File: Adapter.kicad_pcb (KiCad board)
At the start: 6 copper layers, 164.7 x 117 mm, 203 parts, among them J1 GD820HTX75P6HB, J2 2-338069-0, U1 R-78E3.3-1.0, U11 LMV7219M5, U2 LM1117GS-3.3, U5 ADuM1200AR

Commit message: Добавил температурные контуры звщиты
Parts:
- added C50: 0.1u, Capacitor_SMD:C_0805_2012Metric_Pad1.18x1.45mm_HandSolder, B.Cu at (121.2, 108.1)
- added C51: 0.1u, Capacitor_SMD:C_0805_2012Metric_Pad1.18x1.45mm_HandSolder, B.Cu at (121.2, 115.5)
- added C52: 0.1u, Capacitor_SMD:C_0805_2012Metric_Pad1.18x1.45mm_HandSolder, B.Cu at (117.1, 115.5)
- added C53: 0.1u, Capacitor_SMD:C_0805_2012Metric_Pad1.18x1.45mm_HandSolder, B.Cu at (168.1, 108.2)
- added C54: 0.1u, Capacitor_SMD:C_0805_2012Metric_Pad1.18x1.45mm_HandSolder, B.Cu at (168.1, 115.6)
- added C55: 0.1u, Capacitor_SMD:C_0805_2012Metric_Pad1.18x1.45mm_HandSolder, B.Cu at (164.1, 115.6)
- added C56: 0.1u, Capacitor_SMD:C_0805_2012Metric_Pad1.18x1.45mm_HandSolder, B.Cu at (215.4, 108.0)
- added C75: 0.1u, Capacitor_SMD:C_0805_2012Metric_Pad1.18x1.45mm_HandSolder, B.Cu at (215.4, 115.3)
- added C76: 0.1u, Capacitor_SMD:C_0805_2012Metric_Pad1.18x1.45mm_HandSolder, B.Cu at (211.3, 115.3)
- added R56: 1k, Resistor_SMD:R_0805_2012Metric_Pad1.20x1.40mm_HandSolder, B.Cu at (121.2, 117.8)
- added R57: 1k, Resistor_SMD:R_0805_2012Metric_Pad1.20x1.40mm_HandSolder, B.Cu at (117.1, 108.1)
- added R58: 1k, Resistor_SMD:R_0805_2012Metric_Pad1.20x1.40mm_HandSolder, B.Cu at (117.1, 120.1)
- added R59: 1k, Resistor_SMD:R_0805_2012Metric_Pad1.20x1.40mm_HandSolder, B.Cu at (117.1, 117.8)
- added R60: 1k, Resistor_SMD:R_0805_2012Metric_Pad1.20x1.40mm_HandSolder, B.Cu at (168.1, 117.9)
- added R63: 1k, Resistor_SMD:R_0805_2012Metric_Pad1.20x1.40mm_HandSolder, B.Cu at (164.1, 108.2)
- added R64: 1k, Resistor_SMD:R_0805_2012Metric_Pad1.20x1.40mm_HandSolder, B.Cu at (164.1, 120.1)
- added R65: 1k, Resistor_SMD:R_0805_2012Metric_Pad1.20x1.40mm_HandSolder, B.Cu at (164.1, 117.9)
- added R70: 1k, Resistor_SMD:R_0805_2012Metric_Pad1.20x1.40mm_HandSolder, B.Cu at (215.4, 117.6)
- added R72: 1k, Resistor_SMD:R_0805_2012Metric_Pad1.20x1.40mm_HandSolder, B.Cu at (211.3, 108.0)
- added R75: 1k, Resistor_SMD:R_0805_2012Metric_Pad1.20x1.40mm_HandSolder, B.Cu at (211.3, 119.9)
- added R76: 1k, Resistor_SMD:R_0805_2012Metric_Pad1.20x1.40mm_HandSolder, B.Cu at (211.3, 117.6)
- added U3: LMV331, Package_TO_SOT_SMD:SOT-23-5_HandSoldering, B.Cu at (119.1, 111.8)
- added U4: LMV331, Package_TO_SOT_SMD:SOT-23-5_HandSoldering, B.Cu at (166.1, 111.8)
- added U6: LMV331, Package_TO_SOT_SMD:SOT-23-5_HandSoldering, B.Cu at (213.4, 111.5)
- C2, C21, C23, C25, C32, C33: moved to B.Cu
- moved C33 288.8 mm to (233.9, 139.2), turned to 90 degrees
- moved C32 280.1 mm to (231.9, 132.6), turned to 0 degrees
- moved U1 278.7 mm to (230.7, 135.5), turned to -90 degrees
- moved R39 255.3 mm to (190.0, 59.2)
- moved R40 255.3 mm to (190.0, 61.7)
- moved C2 231.9 mm to (195.6, 54.3), turned to -90 degrees
- moved C25 217.3 mm to (204.2, 140.2), turned to -90 degrees
- moved C26 215.3 mm to (204.5, 134.4), turned to -90 degrees
- moved R4 211.1 mm to (202.2, 134.4), turned to 90 degrees
- moved C45 210.6 mm to (190.0, 53.8)
- moved C46 210.6 mm to (190.0, 56.4)
- moved C23 174.8 mm to (157.2, 140.2), turned to -90 degrees
- moved C24 171.9 mm to (157.5, 134.4), turned to -90 degrees
- moved R3 166.1 mm to (155.2, 134.4), turned to 90 degrees
- moved C21 135.6 mm to (110.2, 140.2), turned to -90 degrees
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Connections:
- C1 pad 2: GND -> T1
- C12 pad 2: GND -> T1
- C13 pad 2: GND -> T1
- C16 pad 2: GND -> T1
- C18 pad 2: GND -> T1
- C19 pad 2: GND -> T1
- C2 pad 2: GND -> T1
- C21 pad 2: GND -> T1
- C22 pad 2: GND -> T1
- C23 pad 2: GND -> T1
- C24 pad 1: Current_A_out -> Current_B_out
- C24 pad 2: GND -> T1
- C25 pad 2: GND -> T1
- C26 pad 1: Current_A_out -> Current_C_out
- C26 pad 2: GND -> T1
- C29 pad 1: T3 -> T5
- C32 pad 2: GND -> T1
- C33 pad 2: GND -> T1
- C34 pad 2: GND -> T1
- C35 pad 2: GND -> T1
- C37 pad 2: GND -> T1
- C38 pad 2: GND -> T1
- C39 pad 2: GND -> T1
- C4 pad 2: GND -> T1
- C41 pad 2: GND -> T1
- C42 pad 2: GND -> T1
- C45 pad 2: GND -> T1
- C46 pad 2: GND -> T1
- C47 pad 2: GND -> T1
- C48 pad 2: GND -> T1
- C5 pad 2: GND -> T1
- C57 pad 1: GND -> T1
- C58 pad 1: GND -> T1
- C59 pad 1: GND -> T1
- C6 pad 2: GND -> T1
- C60 pad 1: GND -> T1
- C63 pad 1: GND -> T1
- C64 pad 1: GND -> T1
- C65 pad 1: GND -> T1
- C66 pad 1: GND -> T1
- C69 pad 1: GND -> T1
- C7 pad 2: GND -> T1
- C70 pad 1: GND -> T1
- C71 pad 1: GND -> T1
- C72 pad 1: GND -> T1
- C8 pad 2: GND -> T1
- C9 pad 2: GND -> T1
- D10 pad 1: GND -> T1
- D11 pad 3: GND -> T1
- D13 pad 1: GND -> T1
- D14 pad 3: GND -> T1
- D15 pad 3: GND -> T1
- D16 pad 1: GND -> T1
- D17 pad 1: GND -> T1
- D18 pad 1: GND -> T1
- D19 pad 1: GND -> T1
- D2 pad 2: GND -> T1
- D2 pad 3: GND -> T1
- D2 pad 5: GND -> T1
- D20 pad 5: GND -> T1
- D3 pad 2: GND -> T1
- D3 pad 3: GND -> T1
- D3 pad 5: GND -> T1
- D31 pad 16: GND -> T1
- D31 pad 9: GND -> T1
- D32 pad 16: GND -> T1
- D32 pad 9: GND -> T1
- D37 pad 16: GND -> T1
- D37 pad 9: GND -> T1
- D38 pad 16: GND -> T1
- D38 pad 9: GND -> T1
- D4 pad 1: GND -> T1
- D43 pad 1: GND -> T1
- D44 pad 16: GND -> T1
- D44 pad 9: GND -> T1
- D5 pad 4: unconnected-(D5-DI-Pad4) -> Net-(D1-Y)
- D5 pad 5: GND -> T1
- D6 pad 2: GND -> T1
- D6 pad 3: GND -> T1
- D6 pad 5: GND -> T1
- D64 pad 16: GND -> T1
- D64 pad 9: GND -> T1
- D7 pad 2: GND -> T1
- D7 pad 3: GND -> T1
- D7 pad 5: GND -> T1
- D8 pad 2: GND -> T1
- D8 pad 3: GND -> T1
- D8 pad 5: GND -> T1
- D9 pad 2: GND -> T1
- D9 pad 3: GND -> T1
- D9 pad 5: GND -> T1
- J2 pad 18: GND -> T1
- R28 pad 2: T4 -> T6
- R3 pad 2: Current_A_out -> Current_B_out
- R4 pad 2: Current_A_out -> Current_C_out
- U1 pad 2: GND -> T1
- U11 pad 4: T3 -> T5
- U5 pad 5: GND -> T1
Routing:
- net GND: track 118.4 -> 0.00 mm, vias 2 -> 0
- net (no net): track 582.5 -> 697.8 mm
- net T1: track 0.00 -> 3.07 mm, vias 0 -> 2

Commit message: Убрал питание 3.3В
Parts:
- removed C50, C51, C52, C53, C54, C55, C56, C75, C76: 0.1u, Capacitor_SMD:C_0805_2012Metric_Pad1.18x1.45mm_HandSolder
- removed R56, R57, R58, R59, R60, R63, R64, R65, R70, R72, R75, R76: 1k, Resistor_SMD:R_0805_2012Metric_Pad1.20x1.40mm_HandSolder
- removed U3, U4, U6: LMV331, Package_TO_SOT_SMD:SOT-23-5_HandSoldering
- added D1: SN74AHC1G08DBVR, Package_TO_SOT_SMD:SOT-23-5_HandSoldering, F.Cu at (184.1, 56.7)
- U11: value LMV7219M5 -> LMV7239M5/NOPB
- U2: value LM1117GS-3.3 -> LM1117GS-5.0
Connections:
- net +3.3VA renamed +5VP
- C1 pad 1: +3V3 -> +5V
- C1 pad 2: T1 -> GND
- C12 pad 2: T1 -> GND
- C13 pad 2: T1 -> GND
- C16 pad 2: T1 -> GND
- C18 pad 2: T1 -> GND
- C19 pad 2: T1 -> GND
- C2 pad 1: +3V3 -> +5V
- C2 pad 2: T1 -> GND
- C21 pad 2: T1 -> GND
- C22 pad 2: T1 -> GND
- C23 pad 2: T1 -> GND
- C24 pad 2: T1 -> GND
- C25 pad 2: T1 -> GND
- C26 pad 2: T1 -> GND
- C32 pad 2: T1 -> GND
- C33 pad 1: +3V3 -> +5V
- C33 pad 2: T1 -> GND
- C34 pad 1: +3V3 -> +5V
- C34 pad 2: T1 -> GND
- C35 pad 1: +3V3 -> +5V
- C35 pad 2: T1 -> GND
- C37 pad 2: T1 -> GND
- C38 pad 2: T1 -> GND
- C39 pad 2: T1 -> GND
- C4 pad 2: T1 -> GND
- C41 pad 1: +3V3 -> +5V
- C41 pad 2: T1 -> GND
- C42 pad 1: +3V3 -> +5V
- C42 pad 2: T1 -> GND
- C45 pad 2: T1 -> GND
- C46 pad 2: T1 -> GND
- C47 pad 2: T1 -> GND
- C48 pad 2: T1 -> GND
- C5 pad 1: +3V3 -> +5V
- C5 pad 2: T1 -> GND
- C57 pad 1: T1 -> GND
- C57 pad 2: +3V3 -> +5V
- C58 pad 1: T1 -> GND
- C58 pad 2: +3V3 -> +5V
- C59 pad 1: T1 -> GND
- C6 pad 1: +3V3 -> +5V
- C6 pad 2: T1 -> GND
- C60 pad 1: T1 -> GND
- C63 pad 1: T1 -> GND
- C63 pad 2: +3V3 -> +5V
- C64 pad 1: T1 -> GND
- C64 pad 2: +3V3 -> +5V
- C65 pad 1: T1 -> GND
- C66 pad 1: T1 -> GND
- C69 pad 1: T1 -> GND
- C69 pad 2: +3V3 -> +5V
- C7 pad 1: +3V3 -> +5V
- C7 pad 2: T1 -> GND
- C70 pad 1: T1 -> GND
- C70 pad 2: +3V3 -> +5V
- C71 pad 1: T1 -> GND
- C72 pad 1: T1 -> GND
- C8 pad 1: +3V3 -> +5V
- C8 pad 2: T1 -> GND
- C9 pad 2: T1 -> GND
- D10 pad 1: T1 -> GND
- D11 pad 3: T1 -> GND
- D13 pad 1: T1 -> GND
- D14 pad 3: T1 -> GND
- D15 pad 3: T1 -> GND
- D16 pad 1: T1 -> GND
- D17 pad 1: T1 -> GND
- D18 pad 1: T1 -> GND
- D19 pad 1: T1 -> GND
- D2 pad 2: T1 -> GND
- D2 pad 3: T1 -> GND
- D2 pad 5: T1 -> GND
- D2 pad 8: +3V3 -> +5V
- D20 pad 2: +3V3 -> +5V
- D20 pad 3: +3V3 -> +5V
- D20 pad 5: T1 -> GND
- D20 pad 8: +3V3 -> +5V
- D3 pad 2: T1 -> GND
- D3 pad 3: T1 -> GND
- D3 pad 5: T1 -> GND
- D3 pad 8: +3V3 -> +5V
- D31 pad 15: +3V3 -> +5V
- D31 pad 16: T1 -> GND
- D31 pad 9: T1 -> GND
- D32 pad 15: +3V3 -> +5V
- D32 pad 16: T1 -> GND
- D32 pad 9: T1 -> GND
- D37 pad 15: +3V3 -> +5V
- D37 pad 16: T1 -> GND
- D37 pad 9: T1 -> GND
- D38 pad 15: +3V3 -> +5V
- D38 pad 16: T1 -> GND
- D38 pad 9: T1 -> GND
- D4 pad 1: T1 -> GND
- D43 pad 1: T1 -> GND
- D44 pad 15: +3V3 -> +5V
- D44 pad 16: T1 -> GND
- D44 pad 9: T1 -> GND
- D5 pad 2: +3V3 -> +5V
- D5 pad 3: +3V3 -> +5V
- D5 pad 5: T1 -> GND
- D5 pad 8: +3V3 -> +5V
- D6 pad 2: T1 -> GND
- D6 pad 3: T1 -> GND
- D6 pad 5: T1 -> GND
- D6 pad 8: +3V3 -> +5V
- D64 pad 15: +3V3 -> +5V
- D64 pad 16: T1 -> GND
- D64 pad 9: T1 -> GND
- D7 pad 2: T1 -> GND
- D7 pad 3: T1 -> GND
- D7 pad 5: T1 -> GND
- D7 pad 8: +3V3 -> +5V
- D8 pad 2: T1 -> GND
- D8 pad 3: T1 -> GND
- D8 pad 5: T1 -> GND
- D8 pad 8: +3V3 -> +5V
- D9 pad 2: T1 -> GND
- D9 pad 3: T1 -> GND
- D9 pad 5: T1 -> GND
- D9 pad 8: +3V3 -> +5V
- J2 pad 18: T1 -> GND
- R37 pad 2: +3V3 -> +5V
- R39 pad 2: +3V3 -> +5V
- R40 pad 2: +3V3 -> +5V
- U1 pad 2: T1 -> GND
- U1 pad 3: +3V3 -> +5V
- U5 pad 5: T1 -> GND
- U5 pad 8: +3V3 -> +5V
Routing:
- net Net-(U11-+): track 20.1 -> 0.00 mm
- net Net-(U5-VIA): track 17.7 -> 0.00 mm
- net -15V_L3: track 25.7 -> 9.78 mm, vias 5 -> 0
- net +3V3: track 15.2 -> 0.00 mm, vias 2 -> 0
- net +5VP: track 11.3 -> 0.00 mm, vias 4 -> 0
- net T3: track 90.3 -> 80.0 mm, vias 1 -> 0
- net Temp_N: track 171.3 -> 163.0 mm, vias 1 -> 0
- net Temp_P: track 149.9 -> 144.1 mm, vias 1 -> 0
- net Net-(D20-DI): track 4.74 -> 0.55 mm
- net T1: track 3.07 -> 0.00 mm, vias 2 -> 0
- net E6: track 2.17 -> 0.00 mm, vias 1 -> 0
- net +5V: track 0.00 -> 0.55 mm

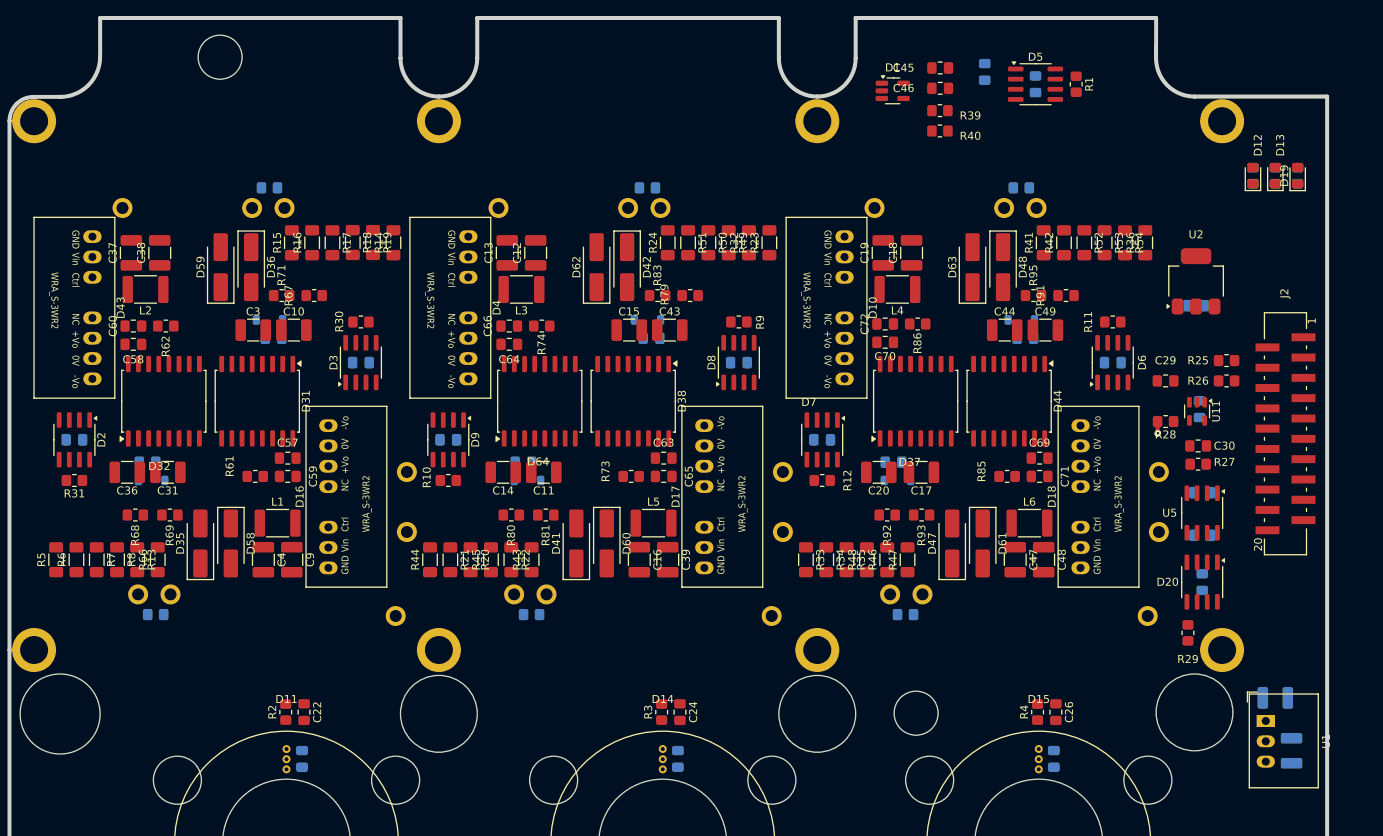
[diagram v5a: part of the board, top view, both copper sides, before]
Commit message: Развел стойку фазы А
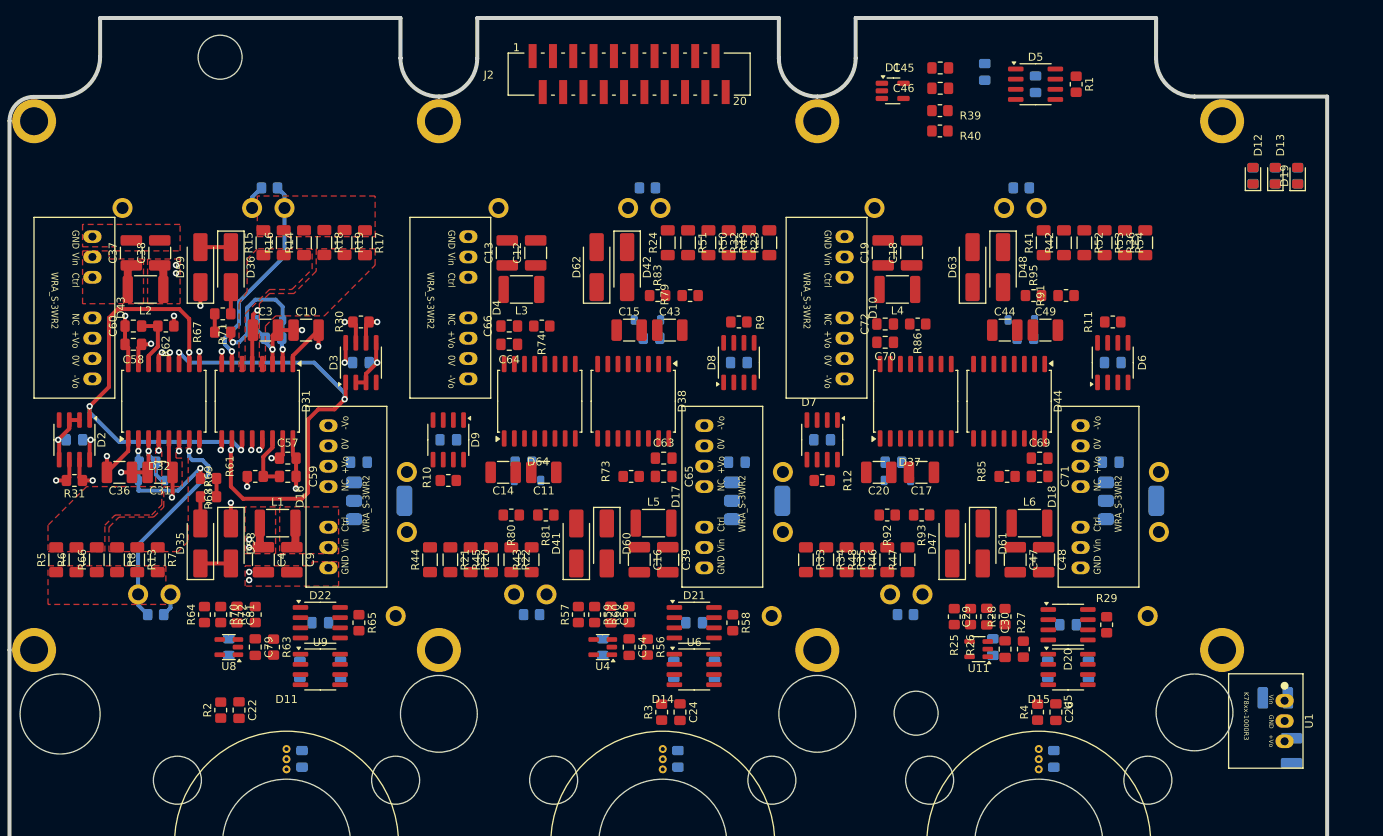
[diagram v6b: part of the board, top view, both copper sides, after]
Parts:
- added C50: 2.2u, Capacitor_SMD:C_0805_2012Metric_Pad1.18x1.45mm_HandSolder, B.Cu at (147.8, 126.2)
- added C51: 2.2u, Capacitor_SMD:C_0805_2012Metric_Pad1.18x1.45mm_HandSolder, B.Cu at (159.3, 123.2)
- added C52: 2.2u, Capacitor_SMD:C_0805_2012Metric_Pad1.18x1.45mm_HandSolder, B.Cu at (156.7, 129.0)
- added C53: 2.2u, Capacitor_SMD:C_0805_2012Metric_Pad1.18x1.45mm_HandSolder, B.Cu at (161.8, 129.0)
- added C54: 56p, Capacitor_SMD:C_0805_2012Metric_Pad1.18x1.45mm_HandSolder, F.Cu at (151.1, 126.2)
- added C55: 2.2u, Capacitor_SMD:C_0805_2012Metric_Pad1.18x1.45mm_HandSolder, B.Cu at (164.6, 103.1)
- added C56: 10n, Capacitor_SMD:C_0805_2012Metric_Pad1.18x1.45mm_HandSolder, F.Cu at (148.8, 122.2)
- added C75: 2.2u, Capacitor_SMD:C_0805_2012Metric_Pad1.18x1.45mm_HandSolder, B.Cu at (101.1, 126.2)
- added C76: 2.2u, Capacitor_SMD:C_0805_2012Metric_Pad1.18x1.45mm_HandSolder, B.Cu at (112.5, 123.2)
- added C77: 2.2u, Capacitor_SMD:C_0805_2012Metric_Pad1.18x1.45mm_HandSolder, B.Cu at (110.0, 129.0)
- added C78: 2.2u, Capacitor_SMD:C_0805_2012Metric_Pad1.18x1.45mm_HandSolder, B.Cu at (115.1, 129.0)
- added C79: 56p, Capacitor_SMD:C_0805_2012Metric_Pad1.18x1.45mm_HandSolder, F.Cu at (104.4, 126.2)
- added C80: 2.2u, Capacitor_SMD:C_0805_2012Metric_Pad1.18x1.45mm_HandSolder, B.Cu at (117.3, 103.1)
- added C81: 10n, Capacitor_SMD:C_0805_2012Metric_Pad1.18x1.45mm_HandSolder, F.Cu at (102.1, 122.2)
- added D21: ADM3485E, Package_SO:SOIC-8_3.9x4.9mm_P1.27mm, F.Cu at (159.3, 123.2)
- added D22: ADM3485E, Package_SO:SOIC-8_3.9x4.9mm_P1.27mm, F.Cu at (112.5, 123.2)
- added R56: 10k, Resistor_SMD:R_0805_2012Metric_Pad1.20x1.40mm_HandSolder, F.Cu at (153.4, 126.2)
- added R57: 10k, Resistor_SMD:R_0805_2012Metric_Pad1.20x1.40mm_HandSolder, F.Cu at (144.8, 122.2)
- added R58: 120, Resistor_SMD:R_0805_2012Metric_Pad1.20x1.40mm_HandSolder, F.Cu at (164.1, 123.2)
- added R59: 10k, Resistor_SMD:R_0805_2012Metric_Pad1.20x1.40mm_HandSolder, F.Cu at (146.8, 122.2)
- added R60: 2.2k, Resistor_SMD:R_0805_2012Metric_Pad1.20x1.40mm_HandSolder, F.Cu at (151.1, 122.2)
- added R63: 10k, Resistor_SMD:R_0805_2012Metric_Pad1.20x1.40mm_HandSolder, F.Cu at (106.7, 126.2)
- added R64: 10k, Resistor_SMD:R_0805_2012Metric_Pad1.20x1.40mm_HandSolder, F.Cu at (98.0, 122.2)
- added R65: 120, Resistor_SMD:R_0805_2012Metric_Pad1.20x1.40mm_HandSolder, F.Cu at (117.3, 123.2)
- added R70: 10k, Resistor_SMD:R_0805_2012Metric_Pad1.20x1.40mm_HandSolder, F.Cu at (100.1, 122.2)
- added R72: 2.2k, Resistor_SMD:R_0805_2012Metric_Pad1.20x1.40mm_HandSolder, F.Cu at (104.4, 122.2)
- added U3: LM1117GS-5.0, Package_TO_SOT_SMD:SOT-223, B.Cu at (167.1, 108.0)
- added U4: LMV7239M5/NOPB, Package_TO_SOT_SMD:SOT-23-5, F.Cu at (147.8, 126.2)
- added U6: ADuM1200AR, Package_SO:SOIC-8_3.9x4.9mm_P1.27mm, F.Cu at (159.3, 129.0)
- added U7: LM1117GS-5.0, Package_TO_SOT_SMD:SOT-223, B.Cu at (119.9, 108.0)
- added U8: LMV7239M5/NOPB, Package_TO_SOT_SMD:SOT-23-5, F.Cu at (101.1, 126.2)
- added U9: ADuM1200AR, Package_SO:SOIC-8_3.9x4.9mm_P1.27mm, F.Cu at (112.5, 129.0)
- U1: value R-78E3.3-1.0 -> K7805-1000R3; footprint Converter_DCDC:Converter_DCDC_RECOM_R-78E-0.5_THT -> DCDC_My:K78xx-1000R3
- U2: moved to B.Cu
- moved J2 96.8 mm to (139.1, 56.9), turned to 0 degrees
- moved R25 46.7 mm to (191.8, 122.4), turned to 90 degrees
- moved R26 43.5 mm to (193.8, 122.4), turned to -90 degrees
- moved U11 40.4 mm to (194.8, 126.5), turned to 180 degrees
- moved C28 39.4 mm to (196.6, 126.2)
- moved C29 37.0 mm to (195.8, 122.4), turned to -90 degrees
- moved C30 35.0 mm to (198.1, 126.5), turned to -90 degrees
- moved R27 31.8 mm to (200.4, 126.5), turned to -90 degrees
- moved R28 31.6 mm to (198.1, 122.4), turned to 90 degrees
- moved C40 29.3 mm to (203.5, 129.0), turned to -90 degrees
- moved U2 28.6 mm to (213.9, 108.0), turned to 0 degrees
- moved U5 25.8 mm to (206.0, 129.0), turned to 0 degrees
- moved C27 22.3 mm to (211.3, 103.1)
- moved C41 22.0 mm to (208.5, 129.0), turned to -90 degrees
- moved C42 17.6 mm to (206.0, 123.4), turned to 0 degrees
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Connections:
- net +5VP renamed +5V_C
- C27 pad 2: -15V_L3 -> -15V_L1
- C28 pad 2: -15V_L3 -> -15V_L1
- C29 pad 2: -15V_L3 -> -15V_L1
- C40 pad 2: -15V_L3 -> -15V_L1
- C43 pad 2: -15V_L2 -> -15V_L1
- C49 pad 2: -15V_L3 -> -15V_L1
- D17 pad 8: -15V_L2 -> -15V_L1
- D18 pad 8: -15V_L3 -> -15V_L1
- D31 pad 12: RDY_L1 -> RDY
- D31 pad 13: FLT_L1 -> FLT
- D32 pad 12: RDY_H1 -> RDY
- D32 pad 13: FLT_H1 -> FLT
- D37 pad 12: RDY_H3 -> RDY
- D37 pad 13: FLT_H3 -> FLT
- D38 pad 1: -15V_L2 -> -15V_L1
- D38 pad 12: RDY_L2 -> RDY
- D38 pad 13: FLT_L2 -> FLT
- D38 pad 8: -15V_L2 -> -15V_L1
- D44 pad 1: -15V_L3 -> -15V_L1
- D44 pad 12: RDY_L3 -> RDY
- D44 pad 13: FLT_L3 -> FLT
- D44 pad 8: -15V_L3 -> -15V_L1
- D64 pad 12: RDY_H2 -> RDY
- D64 pad 13: FLT_H2 -> FLT
- R26 pad 1: -15V_L3 -> -15V_L1
- R61 pad 1: PWM_L1 -> ~{RST}
- R62 pad 1: PWM_H1 -> ~{RST}
- R73 pad 1: PWM_L2 -> ~{RST}
- R74 pad 1: PWM_H2 -> ~{RST}
- R85 pad 1: PWM_L3 -> ~{RST}
- R86 pad 1: PWM_H3 -> ~{RST}
- U11 pad 2: -15V_L3 -> -15V_L1
- U2 pad 1: -15V_L3 -> -15V_L1
- U5 pad 4: -15V_L3 -> -15V_L1
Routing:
- net (no net): track 697.8 -> 0.00 mm
- net unconnected-(J2-Pad20): track 404.3 -> 0.00 mm
- net PWM2_L_P: track 216.9 -> 0.00 mm
- net FLT_L3: track 181.9 -> 0.00 mm
- net RDY_L3: track 177.1 -> 0.00 mm
- net Temp_N: track 163.0 -> 0.00 mm
- net Temp_P: track 144.1 -> 0.00 mm
- net RDY_H3: track 140.7 -> 0.00 mm
- net FLT_H3: track 129.1 -> 0.00 mm
- net RDY_L2: track 105.6 -> 0.00 mm
- net FLT_L2: track 99.4 -> 0.00 mm
- net PWM3_H_N: track 98.4 -> 0.00 mm
- net FLT_H2: track 83.9 -> 0.00 mm
- net T3: track 80.0 -> 0.00 mm
- net PWM_L3: track 79.0 -> 0.00 mm
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- added copper zone on F.Cu, net +15V
- added copper zone on In1.Cu, net +15V_H1
- added copper zone on In1.Cu, net +15V_L1
- added copper zone on In1.Cu, net -15V_H1
- added copper zone on In1.Cu, net -15V_L1
- added copper zone on In2.Cu, net E1
- added copper zone on In2.Cu, net E2
- added copper zone on F.Cu, net G1
- added copper zone on F.Cu, net G2
- added copper zone on F.Cu, net GND
- added copper zone on F.Cu, net Net-(D16-Vin)
- added copper zone on F.Cu, net Net-(D31-OUTH)
- added copper zone on F.Cu, net Net-(D31-OUTL)
- added copper zone on F.Cu, net Net-(D32-OUTH)
- added copper zone on F.Cu, net Net-(D32-OUTL)
- added copper zone on F.Cu, net Net-(D43-Vin)
- removed copper zone on In1.Cu, net +5V_C
- removed copper zone on In2.Cu, net -15V_L1
